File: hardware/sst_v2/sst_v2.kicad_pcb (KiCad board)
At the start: 4 copper layers, 60 x 90 mm, 110 parts, among them U1 Pico_2_W, U2 ADS131M04IPWR, U3 DS3231SN, Y1 ECS-2520MVLC-081.92-BN-TR

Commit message: hw: Testpads TP1-TP15, Soft-Power MAX16150, Fuel-Gauge MAX17048
Testpads: 15 SMD-Pads D 1,0 mm auf B.Cu (GND, Versorgungen, ADC-Takt,
Referenz, ADC-Eingaenge, IMU-Takt/-Versorgung), nicht bestueckt.

Soft-Power: J_PWR1 entfaellt. MAX16150A schaltet ueber Q_PWR1 (DMG2305UX)
+VBAT -> +VBAT_SW. SW_L ist Ein/Aus- und UI-Taster (PB_IN direkt, BTN_L
ueber RB751S40). GP28 = PWR_OFF (ueber 2N7002 an CLR), Teiler
VBAT_SENSE R19/R20/C29 entfaellt.

Fuel-Gauge: MAX17048 an +VBAT und I2C (0x36) fuer Ladestand und
Lade-Rate, auch bei ausgeschaltetem Geraet mit USB.

Ruhestrom aus: ca. 0,8 uA typ, 6,5 uA max. ERC 0 Fehler, DRC 0 Fehler,
0 offene Verbindungen, 0 Paritaetsfehler. Fertigungsdaten, BOM, CPL neu.

Co-Authored-By: Claude Opus 5.5 <noreply@anthropic.com>
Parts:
- removed C29: 100nF X7R, Capacitor_SMD:C_0603_1608Metric
- removed J_PWR1: JST SH 2-pin (PWR switch), Connector_JST:JST_SH_BM02B-SRSS-TB_1x02-1MP_P1.00mm_Vertical
- removed R19, R20: 100k, Resistor_SMD:R_0603_1608Metric
- added C_FG1: 100nF X7R, Capacitor_SMD:C_0603_1608Metric, F.Cu at (130.3, 65.6)
- added C_PWR1: 100nF X7R, Capacitor_SMD:C_0603_1608Metric, F.Cu at (126.2, 61.9)
- added D_PWR1: RB751S40, Diode_SMD:D_SOD-523, F.Cu at (128.7, 62.5)
- added Q_PWR1: DMG2305UX, Package_TO_SOT_SMD:SOT-23, F.Cu at (119.6, 82.1)
- added Q_PWR2: 2N7002, Package_TO_SOT_SMD:SOT-23, F.Cu at (126.6, 71.0)
- added Q_PWR3: 2N7002, Package_TO_SOT_SMD:SOT-23, F.Cu at (122.8, 69.0)
- added R_PWR1: 100k, Resistor_SMD:R_0603_1608Metric, F.Cu at (122.9, 82.1)
- added R_PWR2: 100k, Resistor_SMD:R_0603_1608Metric, F.Cu at (129.6, 70.6)
- added R_PWR3: 100k, Resistor_SMD:R_0603_1608Metric, F.Cu at (122.6, 64.7)
- added R_PWR4: 100k, Resistor_SMD:R_0603_1608Metric, F.Cu at (121.9, 72.6)
- added TP1: GND, TestPoint:TestPoint_Pad_D1.0mm, B.Cu at (93.0, 121.0)
- added TP10: EXC, TestPoint:TestPoint_Pad_D1.0mm, B.Cu at (91.0, 87.8)
- added TP11: FORK, TestPoint:TestPoint_Pad_D1.0mm, B.Cu at (100.8, 126.5)
- added TP12: SHCK, TestPoint:TestPoint_Pad_D1.0mm, B.Cu at (100.9, 123.4)
- added TP13: 32K, TestPoint:TestPoint_Pad_D1.0mm, B.Cu at (117.8, 121.7)
- added TP14: IMU, TestPoint:TestPoint_Pad_D1.0mm, B.Cu at (126.5, 134.8)
- added TP15: GND, TestPoint:TestPoint_Pad_D1.0mm, B.Cu at (114.3, 127.2)
- added TP2: GND, TestPoint:TestPoint_Pad_D1.0mm, B.Cu at (110.0, 57.0)
- added TP3: GND, TestPoint:TestPoint_Pad_D1.0mm, B.Cu at (89.8, 126.1)
- added TP4: 3V0A, TestPoint:TestPoint_Pad_D1.0mm, B.Cu at (96.5, 114.0)
- added TP5: DVDD, TestPoint:TestPoint_Pad_D1.0mm, B.Cu at (86.8, 128.7)
- added TP6: CLK, TestPoint:TestPoint_Pad_D1.0mm, B.Cu at (92.3, 126.6)
- added TP7: VBSW, TestPoint:TestPoint_Pad_D1.0mm, B.Cu at (123.4, 106.8)
- added TP8: VBAT, TestPoint:TestPoint_Pad_D1.0mm, B.Cu at (115.7, 52.6)
- added TP9: REF, TestPoint:TestPoint_Pad_D1.0mm, B.Cu at (104.9, 110.2)
- added U_FG1: MAX17048G+T10, Package_DFN_QFN:TDFN-8-1EP_2x2mm_P0.5mm_EP0.8x1.2mm, F.Cu at (133.0, 64.6)
- added U_PWR1: MAX16150AUT+T, Package_TO_SOT_SMD:SOT-23-6, F.Cu at (125.6, 64.7)
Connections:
- SW_L1 pad 2: BTN_L -> PWR_BTN
- U1 pad 34: VBAT_SENSE -> PWR_OFF
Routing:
- net +VBAT: track 16.8 -> 77.1 mm, vias 2 -> 4
- net PWR_BTN: track 0.00 -> 49.6 mm, vias 0 -> 2
- net BTN_L: track 51.4 -> 4.70 mm
- net +VBAT_SW: track 84.5 -> 54.9 mm
- net VBAT_SENSE: track 20.4 -> 0.00 mm
- net PSW_GATE: track 0.00 -> 18.7 mm, vias 0 -> 2
- net unconnected-(J_PWR1-PadMP): track 12.3 -> 0.00 mm
- net PSW_EN: track 0.00 -> 8.93 mm
- net PWR_OFF: track 0.00 -> 7.13 mm, vias 0 -> 1
- net GND: track 50.0 -> 55.1 mm, vias 97 -> 107
- net DISP_SDA: track 70.1 -> 73.4 mm
- net DISP_SCL: track 68.3 -> 70.9 mm
- net PWR_CLR: track 0.00 -> 2.40 mm
- net SHOCK_AIN_P: track 5.30 -> 6.89 mm, vias 0 -> 1
- net FORK_AIN_P: track 5.01 -> 6.01 mm
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
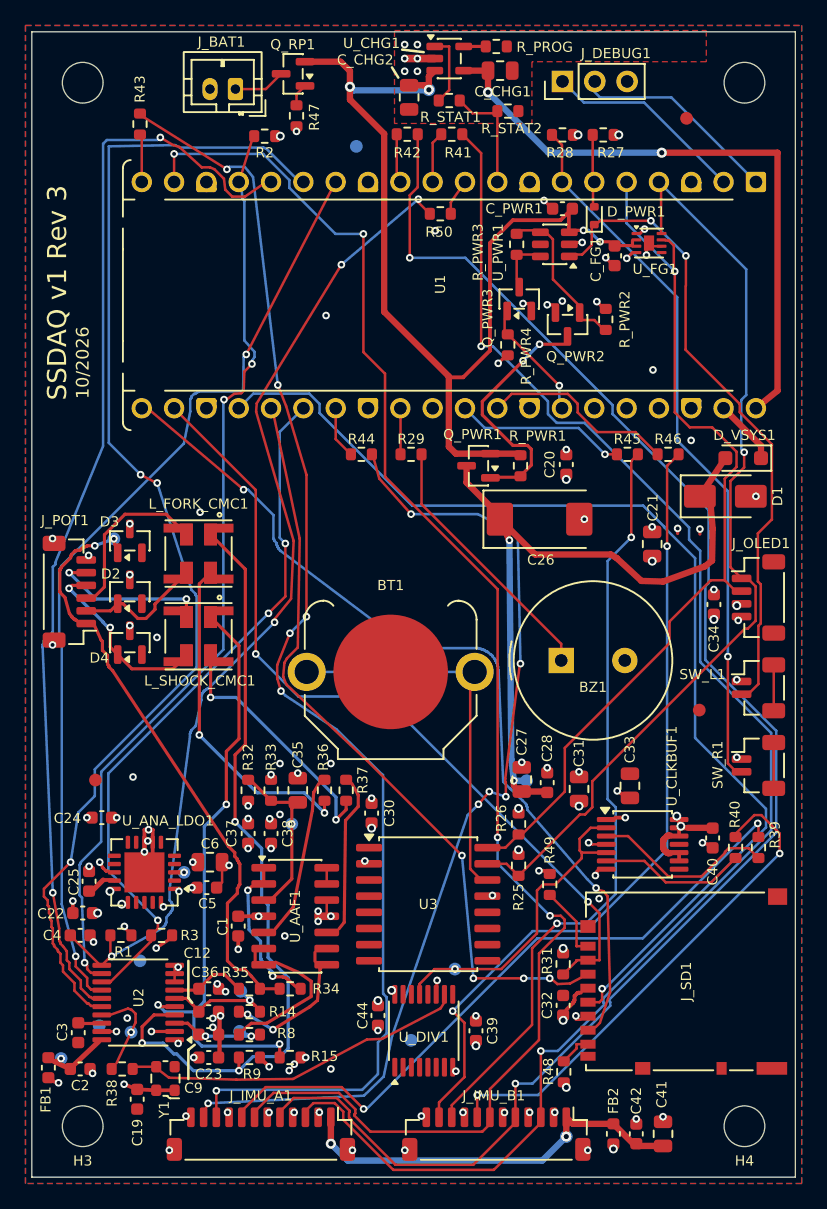
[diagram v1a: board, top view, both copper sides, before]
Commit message: hw: Pico 7 mm nach links, Pico-Netze neu geroutet
U1 von x 141,4 nach 134,4: Antennenende 0,2 mm vor der linken
Platinenkante, USB-Ende bei x 137,1 (7,4 mm Platine davor). Der
90-Grad-Micro-B-Stecker ragt dadurch rund 7 mm weniger ueber die Kante,
das Gehaeuse wird schmaler. Keepout "Pico antenna" mitverschoben
(x 84,5-94,0), R50 direkt an GP7, Platinentexte an den rechten Rand.

Leiterbahnen 2697 -> 2735 mm, Vias 250 -> 264. ERC 0 Fehler, DRC
0 Fehler, 0 offene Verbindungen, 0 Paritaetsfehler. Fertigungsdaten
und CPL neu.

Co-Authored-By: Claude Opus 5.5 <noreply@anthropic.com>
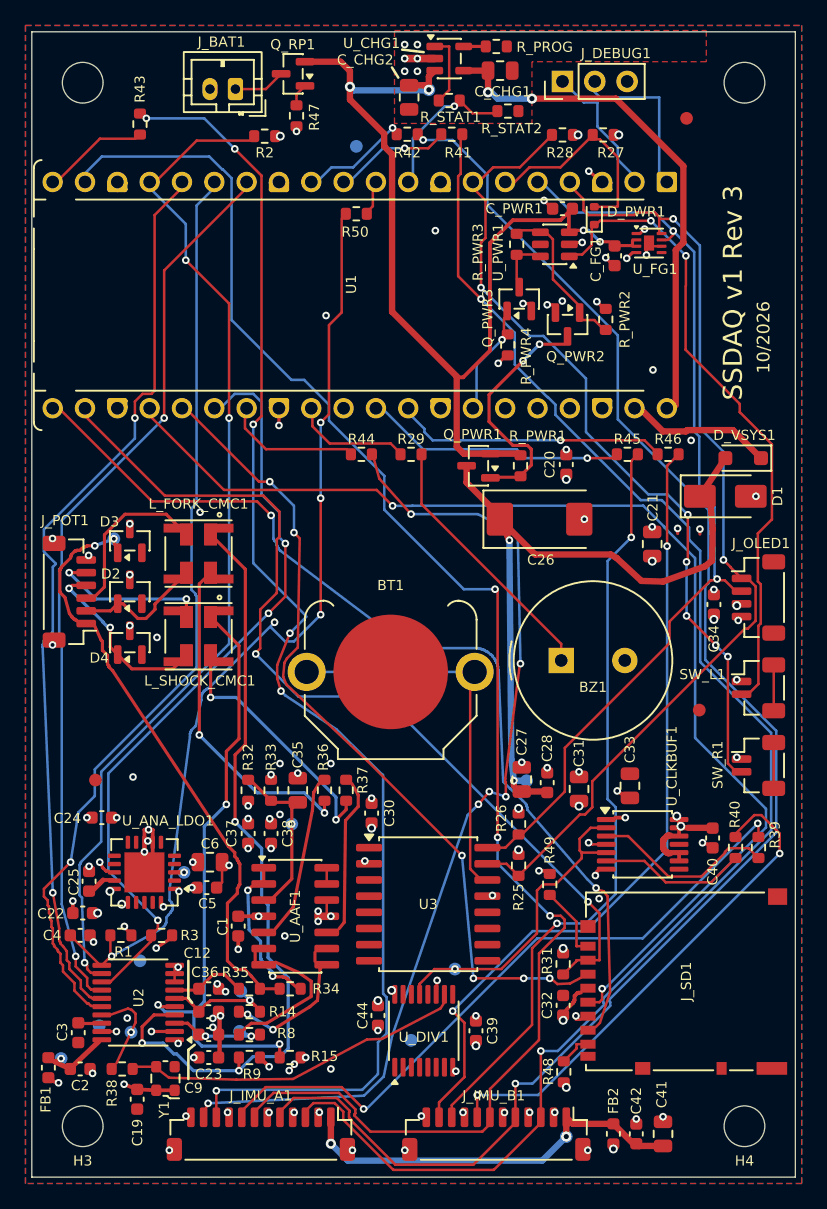
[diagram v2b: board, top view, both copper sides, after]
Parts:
- moved U1 7.00 mm to (134.4, 59.8)
- moved R50 6.60 mm to (110.0, 62.3)
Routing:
- net ADC_SDI: track 91.9 -> 71.5 mm, vias 3 -> 1
- net ADC_SDO: track 84.6 -> 70.3 mm
- net BTN_L: track 4.70 -> 14.9 mm
- net +VBUS: track 49.2 -> 40.2 mm
- net SD_CS: track 64.5 -> 72.5 mm
- net SD_MISO: track 68.2 -> 75.6 mm
- net ADC_CS: track 70.8 -> 77.7 mm
- net BTN_R: track 56.5 -> 62.8 mm, vias 1 -> 6
- net IMU_CS2_MCU: track 13.4 -> 19.4 mm
- net GP1/UART_RX: track 16.8 -> 10.9 mm
- net IMU_CS1_MCU: track 4.11 -> 9.58 mm
- net SD_SCK: track 85.8 -> 91.0 mm, vias 1 -> 2
- net VSYS: track 5.14 -> 10.3 mm
- net IMU_CS3_MCU: track 15.4 -> 20.2 mm, vias 0 -> 1
- net BUZ_DRV_A: track 3.63 -> 8.12 mm
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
